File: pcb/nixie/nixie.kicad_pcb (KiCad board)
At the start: 2 copper layers, 144 x 116 mm, 54 parts, among them J1 Conn_01x02, J2 Conn_01x02, J3 Conn_01x32, J4 Conn_01x32, J5 Conn_01x32, J6 Conn_01x32, J7 Conn_01x04, P1 TTL_232R_3V3, U1 SN74LVC2G17, U10 nixie_8422, U11 nixie_8422, U12 nixie_8422, U13 nixie_8422, U14 SN74LVC2G17, U2 LM317EMP, U3 ESP-WROOM-32, U4 TACTILE, U5 TACTILE, U6 nixie_8422, U7 HV5530, U8 HV5530, U9 nixie_8422

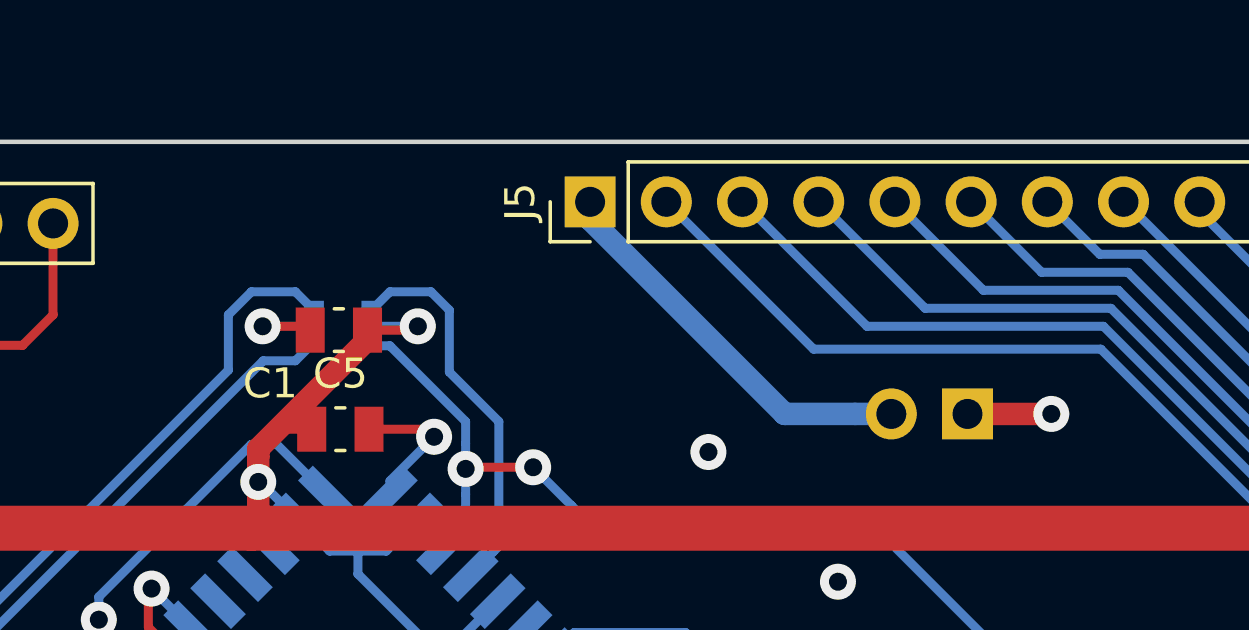
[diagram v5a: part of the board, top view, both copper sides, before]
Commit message: Finished lower part
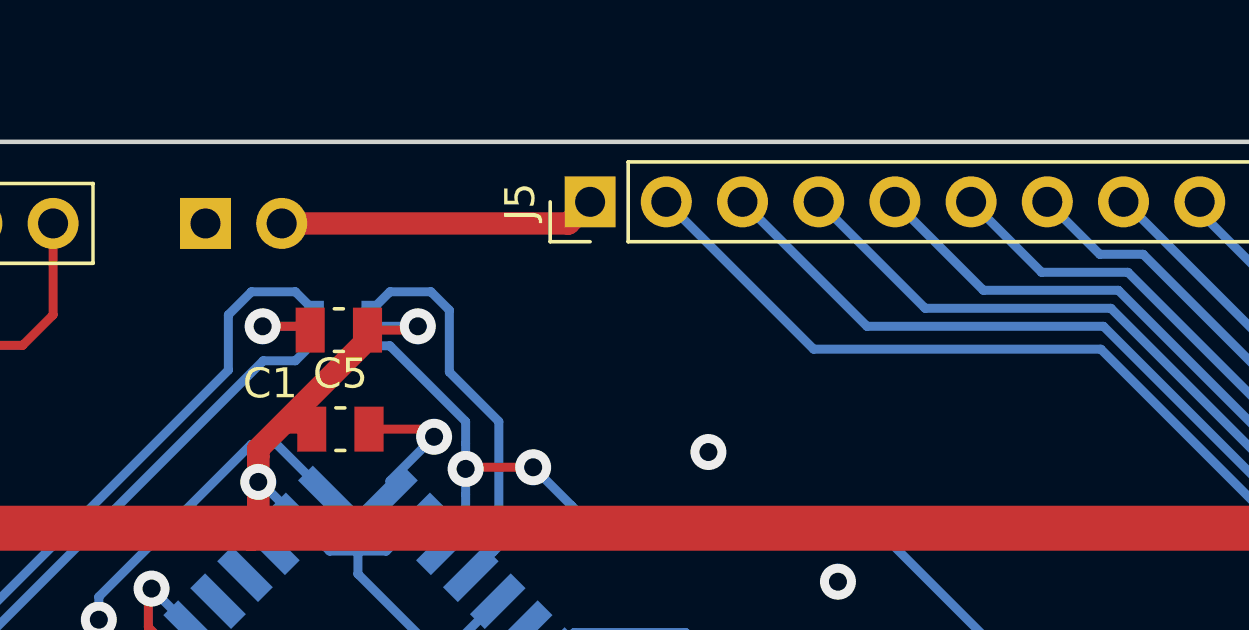
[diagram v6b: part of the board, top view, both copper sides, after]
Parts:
- moved J2 26.2 mm to (69.2, 98.7), turned to 270 degrees
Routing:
- net GND: track 38.5 -> 35.7 mm, vias 38 -> 37
- net HT: track 139.0 -> 136.2 mm
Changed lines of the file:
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@@
-(kicad_pcb (version 20171130) (host pcbnew 5.0.0-rc2-dev-unknown-2bd0a02~65~ubuntu18.04.1)
+(kicad_pcb (version 20171130) (host pcbnew 5.0.0-rc2-dev-unknown-8f6ae70~65~ubuntu18.04.1)
   (general
     (thickness 1.6)
     (drawings 16)
-    (tracks 1088)
+    (tracks 1084)
     (zones 0)
     (modules 54)
@@
   )
   (module Connector_PinHeader_2.54mm:PinHeader_1x02_P2.54mm_Vertical (layer B.Cu)
-    (at 94.58 105.07 90)
+    (at 69.18 98.72 270)
     (descr "Through hole straight pin header, 1x02, 2.54mm pitch, single row")
     (tags "Through hole pin header THT 1x02 2.54mm single row")
-    (fp_text reference J2 (at 0 2.33 90) (layer B.SilkS)
+    (fp_text reference J2 (at 0 2.33 270) (layer B.SilkS)
       (effects (font (size 1 1) (thickness 0.15)) (justify mirror))
     )
-    (fp_text value Conn_01x02 (at 0 -4.87 90) (layer B.Fab)
+    (fp_text value Conn_01x02 (at 0 -4.87 270) (layer B.Fab)
       (effects (font (size 1 1) (thickness 0.15)) (justify mirror))
     )
@@
     (fp_line (start 1.8 -4.35) (end 1.8 1.8) (layer B.CrtYd) (width 0.05))
     (fp_line (start 1.8 1.8) (end -1.8 1.8) (layer B.CrtYd) (width 0.05))
-    (fp_text user %R (at 0 -1.27) (layer B.Fab)
+    (fp_text user %R (at 0 -1.27 180) (layer B.Fab)
       (effects (font (size 1 1) (thickness 0.15)) (justify mirror))
     )
-    (pad 1 thru_hole rect (at 0 0 90) (size 1.7 1.7) (drill 1) (layers *.Cu *.Mask)
+    (pad 1 thru_hole rect (at 0 0 270) (size 1.7 1.7) (drill 1) (layers *.Cu *.Mask)
       (net 76 GND))
-    (pad 2 thru_hole oval (at 0 -2.54 90) (size 1.7 1.7) (drill 1) (layers *.Cu *.Mask)
+    (pad 2 thru_hole oval (at 0 -2.54 270) (size 1.7 1.7) (drill 1) (layers *.Cu *.Mask)
       (net 90 HT))
     (model ${KISYS3DMOD}/Connector_PinHeader_2.54mm.3dshapes/PinHeader_1x02_P2.54mm_Vertical.wrl
@@
   (segment (start 107.4 21.751) (end 108.677 23.028) (width 0.3) (layer B.Cu) (net 61))
   (segment (start 114.526015 46.261985) (end 112.285773 46.261985) (width 0.3) (layer B.Cu) (net 61))
-  (segment (start 87.588 119.548) (end 101.04 133) (width 0.3) (layer B.Cu) (net 63))
-  (segment (start 84.309755 118.839499) (end 85.018256 119.548) (width 0.3) (layer B.Cu) (net 63))
-  (segment (start 85.018256 119.548) (end 87.588 119.548) (width 0.3) (layer B.Cu) (net 63))
-  (segment (start 90.88 132.593948) (end 90.88 133) (width 0.3) (layer B.Cu) (net 64))
-  (segment (start 80.717653 122.431601) (end 90.88 132.593948) (width 0.3) (layer B.Cu) (net 64))
   (segment (start 84.16303 115.051175) (end 84.997546 115.051175) (width 0.3) (layer B.Cu) (net 62))
   (segment (start 105.270001 132.150001) (end 106.12 133) (width 0.3) (layer B.Cu) (net 62))
@@
   (segment (start 91.285773 46.261985) (end 96.985985 46.261985) (width 0.3) (layer B.Cu) (net 62))
   (segment (start 96.985985 46.261985) (end 105.270001 54.546001) (width 0.3) (layer B.Cu) (net 62))
+  (segment (start 87.588 119.548) (end 101.04 133) (width 0.3) (layer B.Cu) (net 63))
+  (segment (start 84.309755 118.839499) (end 85.018256 119.548) (width 0.3) (layer B.Cu) (net 63))
+  (segment (start 85.018256 119.548) (end 87.588 119.548) (width 0.3) (layer B.Cu) (net 63))
   (segment (start 92.353468 52.838011) (end 97.878011 52.838011) (width 0.3) (layer B.Cu) (net 63))
   (segment (start 97.878011 52.838011) (end 100.190001 55.150001) (width 0.3) (layer B.Cu) (net 63))
@@
   (segment (start 83.714227 47.976227) (end 85.610945 49.872945) (width 0.3) (layer B.Cu) (net 63))
   (segment (start 100.190001 55.150001) (end 101.04 56) (width 0.3) (layer B.Cu) (net 63))
+  (segment (start 90.88 132.593948) (end 90.88 133) (width 0.3) (layer B.Cu) (net 64))
+  (segment (start 80.717653 122.431601) (end 90.88 132.593948) (width 0.3) (layer B.Cu) (net 64))
   (segment (start 84.489809 52.272989) (end 87.152989 52.272989) (width 0.3) (layer B.Cu) (net 64))
   (segment (start 78.705 46.48818) (end 84.489809 52.272989) (width 0.3) (layer B.Cu) (net 64))
@@
   (segment (start 140.3 131.74) (end 140.3 129.454) (width 0.75) (layer F.Cu) (net 76))
   (via (at 140.3 129.454) (size 1.2) (drill 0.6) (layers F.Cu B.Cu) (net 76))
-  (via (at 97.374 105.07) (size 1.2) (drill 0.6) (layers F.Cu B.Cu) (net 76))
-  (segment (start 94.58 105.07) (end 97.374 105.07) (width 0.75) (layer F.Cu) (net 76))
   (via (at 36.414 128.438) (size 1.2) (drill 0.6) (layers F.Cu B.Cu) (net 76))
   (via (at 33.366 126.533) (size 1.2) (drill 0.6) (layers F.Cu B.Cu) (net 77))
@@
   (segment (start 59.782 21) (end 59.9 21.118) (width 0.3) (layer B.Cu) (net 90))
   (segment (start 82 98) (end 82 98.332) (width 0.75) (layer F.Cu) (net 90))
-  (segment (start 90.837919 105.07) (end 92.04 105.07) (width 0.75) (layer B.Cu) (net 90))
-  (segment (start 88.484 105.07) (end 90.837919 105.07) (width 0.75) (layer B.Cu) (net 90))
-  (segment (start 82 98) (end 82 98.586) (width 0.75) (layer B.Cu) (net 90))
-  (segment (start 82 98.586) (end 88.484 105.07) (width 0.75) (layer B.Cu) (net 90))
+  (segment (start 81.28 98.72) (end 82 98) (width 0.75) (layer F.Cu) (net 90))
+  (segment (start 71.72 98.72) (end 81.28 98.72) (width 0.75) (layer F.Cu) (net 90))
   (segment (start 68.700373 112.210373) (end 67.38247 110.89247) (width 0.3) (layer B.Cu) (net 95))
   (via (at 67.38247 110.89247) (size 1.2) (drill 0.6) (layers F.Cu B.Cu) (net 95))

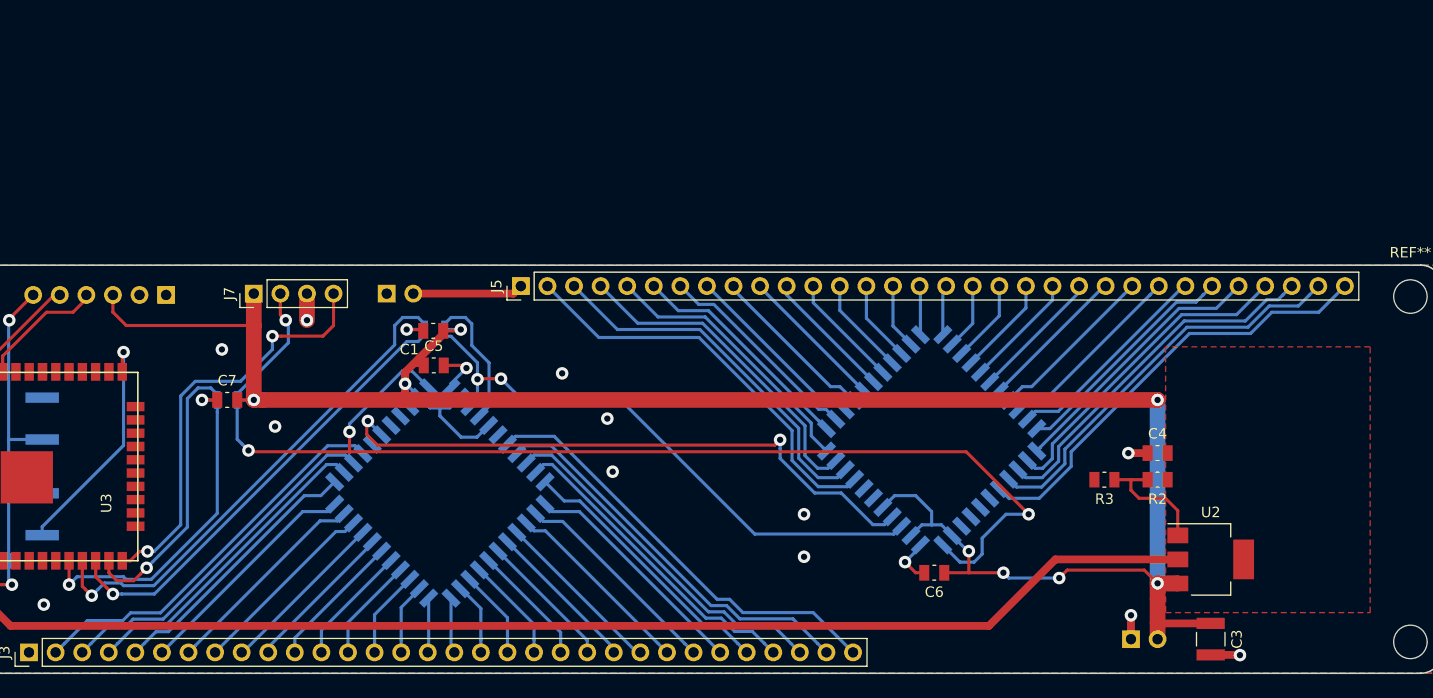
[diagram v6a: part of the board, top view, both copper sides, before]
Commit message: Decided for 12V input voltage
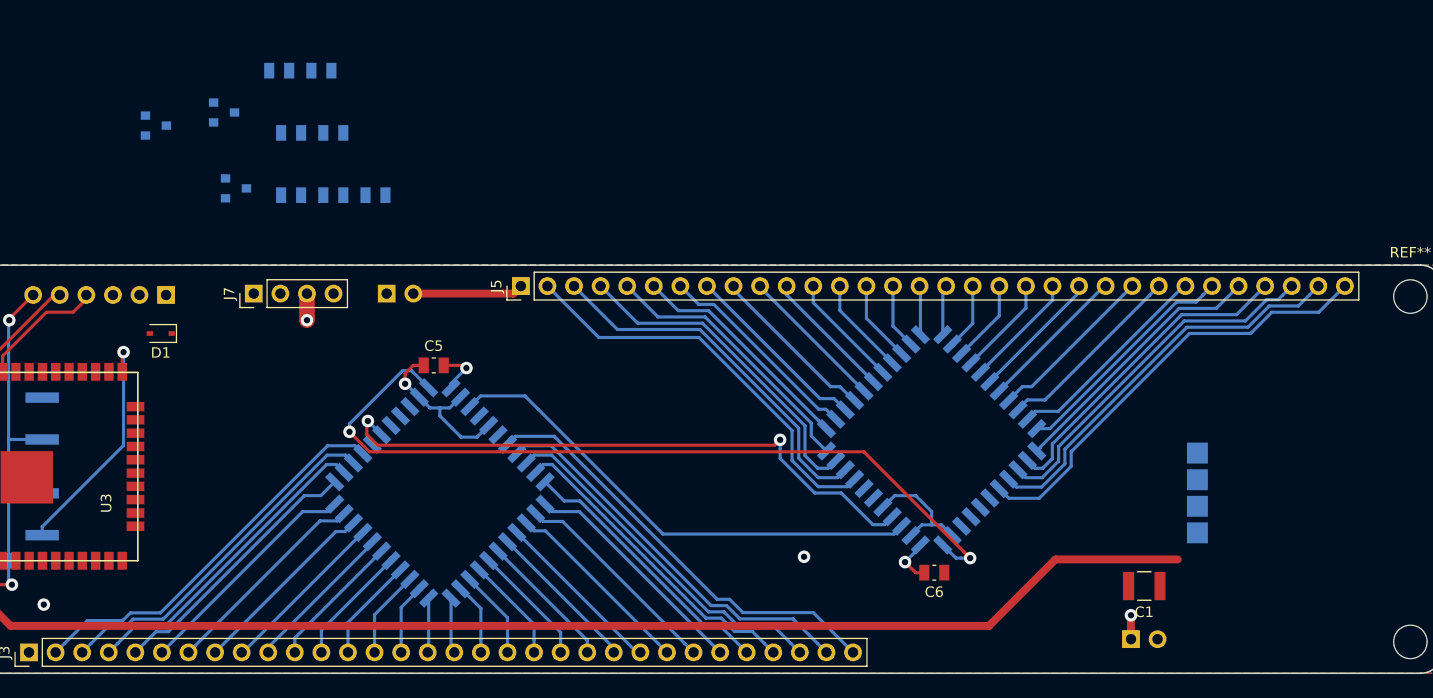
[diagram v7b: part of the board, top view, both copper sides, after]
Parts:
- removed C3: 10u, Capacitor_SMD:C_1210_3225Metric
- removed C4, C7: 1u, Capacitor_SMD:C_0805_2012Metric
- removed U14: SN74LVC2G17, Package_TO_SOT_SMD:SOT-363_SC-70-6
- removed U2: LM317EMP, SOT-223
- added D1: B5819WS, Diode_SMD:D_SOD-323, F.Cu at (47.6, 102.5)
- added Q1: BSS138, Package_TO_SOT_SMD:SOT-23, B.Cu at (53.6, 81.4)
- added Q2: BSS138, Package_TO_SOT_SMD:SOT-23, B.Cu at (54.8, 88.7)
- added Q3: BSS138, Package_TO_SOT_SMD:SOT-23, B.Cu at (47.1, 82.7)
- added R14: 10k, Resistor_SMD:R_0805_2012Metric, B.Cu at (62.9, 77.4)
- added R15: 10k, Resistor_SMD:R_0805_2012Metric, B.Cu at (58.9, 77.4)
- added R16: 10k, Resistor_SMD:R_0805_2012Metric, B.Cu at (68.1, 89.3)
- added R17: 10k, Resistor_SMD:R_0805_2012Metric, B.Cu at (64.1, 83.4)
- added R18: 50R, Resistor_SMD:R_0805_2012Metric, B.Cu at (60.0, 83.4)
- C1: value 1u -> 10u; footprint Capacitor_SMD:C_0805_2012Metric -> Capacitor_SMD:C_1210_3225Metric
- R2: value 590R -> 10k; moved to B.Cu
- R3: value 1k -> 10k; moved to B.Cu
- U1: value SN74LVC2G17 -> DCDC_mod; footprint Package_TO_SOT_SMD:SOT-363_SC-70-6 -> myStuff:ebay_dcdc
- moved R2 87.1 mm to (60.0, 89.3), turned to 0 degrees
- moved U1 78.6 mm to (149.2, 124.1), turned to 180 degrees
- moved R3 78.5 mm to (64.1, 89.3), turned to 0 degrees
- moved C1 72.2 mm to (141.6, 126.7), turned to 180 degrees
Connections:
- C1 pad 1: GND -> +12V
- C1 pad 2: +5V -> GND
- C5 pad 1: +5V -> +12V
- C6 pad 1: +5V -> +12V
- J1 pad 2: +5V -> +12V
- J7 pad 1: +5V -> +3V3
- P1 pad 3: +5V -> Net-(D1-Pad2)
- R2 pad 1: +3V3 -> +12V
- R2 pad 2: Net-(R2-Pad2) -> /tubes/clk
- R3 pad 1: Net-(R2-Pad2) -> +3V3
- R3 pad 2: GND -> Net-(Q1-Pad2)
- U1 pad 1: Net-(U1-Pad1) -> +3V3
- U1 pad 3: Net-(U1-Pad3) -> +12V
- U1 pad 4: /tubes/dat -> +12V
- U3 pad 10: Net-(U14-Pad1) -> Net-(Q1-Pad2)
- U3 pad 11: Net-(U1-Pad3) -> Net-(Q2-Pad2)
- U3 pad 12: Net-(U1-Pad1) -> Net-(Q3-Pad2)
- U3 pad 13: Net-(U14-Pad3) -> Net-(J7-Pad2)
- U7 pad 27: +5V -> +12V
- U7 pad 30: +5V -> +12V
- U7 pad 33: +5V -> +12V
- U8 pad 27: +5V -> +12V
- U8 pad 30: +5V -> +12V
- U8 pad 33: +5V -> +12V
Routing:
- net +5V: track 210.7 -> 0.00 mm, vias 8 -> 0
- net Net-(U1-Pad3): track 48.0 -> 0.00 mm, vias 1 -> 0
- net Net-(U1-Pad1): track 43.8 -> 0.00 mm, vias 1 -> 0
- net Net-(J7-Pad4): track 40.5 -> 0.00 mm, vias 2 -> 0
- net Net-(U14-Pad1): track 29.7 -> 0.00 mm, vias 1 -> 0
- net +12V: track 0.00 -> 28.3 mm, vias 0 -> 1
- net /tubes/clk: track 106.4 -> 78.5 mm, vias 3 -> 2
- net Net-(U14-Pad3): track 26.8 -> 0.00 mm, vias 1 -> 0
- net /tubes/dat: track 12.9 -> 0.00 mm
- net Net-(J7-Pad2): track 11.9 -> 0.00 mm, vias 1 -> 0
- net Net-(R2-Pad2): track 11.8 -> 0.00 mm
- net GND: track 35.7 -> 24.8 mm, vias 37 -> 27
- net /tubes/nLatch: track 55.7 -> 47.5 mm, vias 2 -> 0
- removed copper zone on F.Cu, net +3V3

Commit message: Technically done
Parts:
- R14, R15, R16, R17, R2, R3: moved to F.Cu
- moved Q3 51.9 mm to (93.3, 106.3)
- moved R18 41.5 mm to (43.8, 121.6), turned to 270 degrees
- moved R17 37.2 mm to (93.3, 106.3), turned to 90 degrees
- moved R16 33.6 mm to (97.1, 106.3), turned to 270 degrees
- moved R15 29.0 mm to (60.3, 106.3), turned to 90 degrees
- moved R14 28.9 mm to (62.8, 106.3), turned to 270 degrees
- moved Q1 24.9 mm to (53.9, 106.3)
- moved R3 20.5 mm to (52.7, 106.3), turned to 90 degrees
- moved Q2 18.9 mm to (61.6, 106.3)
- moved R2 17.7 mm to (55.2, 106.3), turned to 270 degrees
- moved U1 15.3 mm to (147.9, 108.9)
- moved C5 9.49 mm to (83.2, 105.1)
- moved C1 5.08 mm to (146.7, 126.7)
- moved J1 5.08 mm to (145.4, 131.7)
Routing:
- net +12V: track 28.3 -> 206.1 mm, vias 1 -> 4
- net Net-(Q3-Pad2): track 0.00 -> 74.5 mm, vias 0 -> 2
- net +3V3: track 126.3 -> 187.9 mm, vias 1 -> 11
- net Net-(J7-Pad4): track 0.00 -> 46.4 mm, vias 0 -> 2
- net Net-(Q2-Pad2): track 0.00 -> 40.7 mm, vias 0 -> 2
- net Net-(Q1-Pad2): track 0.00 -> 39.6 mm, vias 0 -> 3
- net /tubes/clk: track 78.5 -> 105.0 mm, vias 2 -> 4
- net /tubes/dat: track 0.00 -> 24.8 mm, vias 0 -> 2
- net /tubes/nLatch: track 47.5 -> 61.3 mm, vias 0 -> 4
- net Net-(U7-Pad23): track 58.8 -> 69.6 mm
- net GND: track 24.8 -> 34.0 mm, vias 27 -> 32
- net Net-(D1-Pad2): track 0.00 -> 5.94 mm
- net /tubes/n0_0: track 50.9 -> 50.1 mm
- net /tubes/n0_9: track 57.7 -> 56.9 mm
- net /tubes/n0_8: track 64.9 -> 64.1 mm
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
